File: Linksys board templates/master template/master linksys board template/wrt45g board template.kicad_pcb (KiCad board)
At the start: 2 copper layers, 160 x 138 mm, 98 parts, among them J1 RJ45, J2 RJ45, J3 RJ45, J4 RJ45, J5 RJ45, J6 Barrel_Jack_Switch, J7 switched ground, SW1 SW_Push, SW2 SW_Push, U1 AMS1117-3.3, U2 AMS1117-5.0, U3 YAAJ_DCDC_StepDown_LM2596

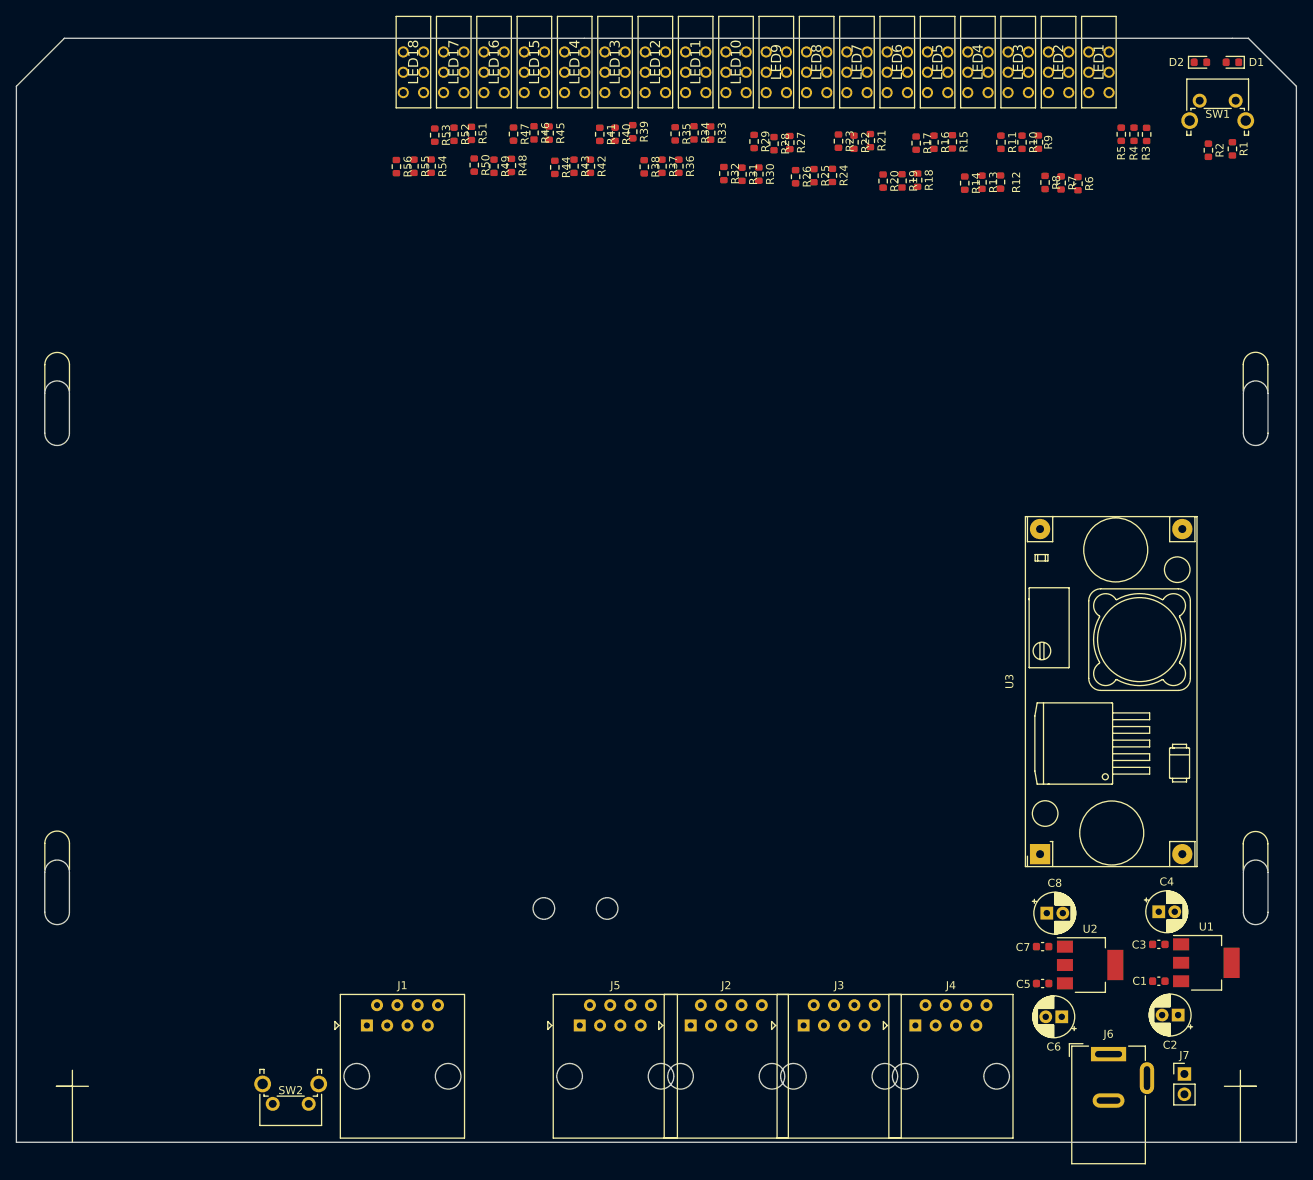
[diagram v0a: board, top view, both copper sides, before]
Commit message: tweaks to locations based on 1:1 printouts
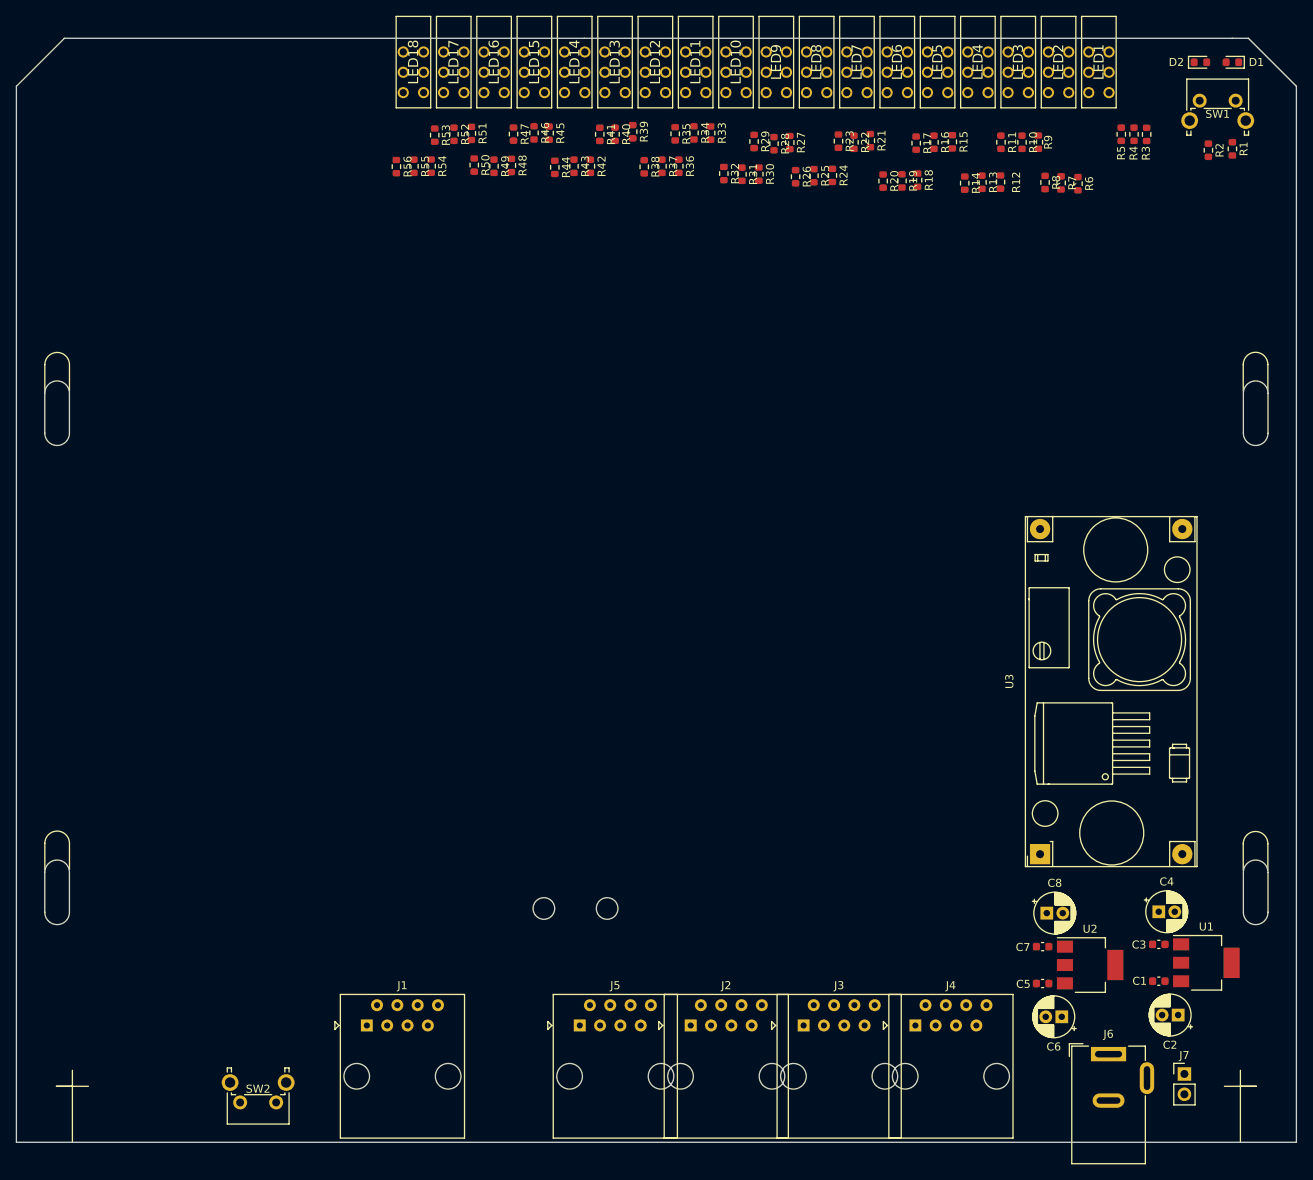
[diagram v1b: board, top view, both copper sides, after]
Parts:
- moved SW2 4.07 mm to (99.5, 155.0)
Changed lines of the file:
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@@
   )
   (footprint "Button_Switch_THT:SW_Tactile_SPST_Angled_PTS645Vx58-2LFS" (layer "F.Cu")
-    (at 103.54 155.2 180)
+    (at 99.47 155.02 180)
     (descr "tactile switch SPST right angle, PTS645VL58-2 LFS")
     (tags "tactile switch SPST angled PTS645VL58-2 LFS C&K Button")
@@
   (gr_line (start 223.435034 126) (end 223.435034 122.689649) (layer "F.SilkS") (width 0.1))
   (gr_line (start 220 160) (end 220 153) (layer "F.SilkS") (width 0.15))
-  (gr_arc (start 70.555001 62.8) (mid 72.1 61.270348) (end 73.635033 62.81) (layer "F.SilkS") (width 0.1))
+  (gr_arc (start 70.555001 62.8) (mid 72.1 61.270347) (end 73.635033 62.81) (layer "F.SilkS") (width 0.1))
   (gr_line (start 220 153) (end 220 151) (layer "F.SilkS") (width 0.15))
   (gr_line (start 74 153) (end 74 151) (layer "F.SilkS") (width 0.15))
   (gr_line (start 220.355002 126) (end 220.355002 122.679649) (layer "F.SilkS") (width 0.1))
   (gr_line (start 70.555001 66.120351) (end 70.555001 62.8) (layer "F.SilkS") (width 0.1))
-  (gr_arc (start 220.355001 62.779649) (mid 221.9 61.249998) (end 223.435033 62.789649) (layer "F.SilkS") (width 0.1))
+  (gr_arc (start 220.355001 62.779649) (mid 221.9 61.249997) (end 223.435033 62.789649) (layer "F.SilkS") (width 0.1))
   (gr_line (start 220 153) (end 222 153) (layer "F.SilkS") (width 0.15))
   (gr_line (start 73.635033 125.950002) (end 73.635033 122.639651) (layer "F.SilkS") (width 0.1))
   (gr_line (start 73.635033 66.120351) (end 73.635033 62.81) (layer "F.SilkS") (width 0.1))
-  (gr_arc (start 220.355002 122.679649) (mid 221.900001 121.149999) (end 223.435034 122.689649) (layer "F.SilkS") (width 0.1))
+  (gr_arc (start 220.355002 122.679649) (mid 221.900001 121.149998) (end 223.435034 122.689649) (layer "F.SilkS") (width 0.1))
   (gr_line (start 223.435033 66.1) (end 223.435033 62.789649) (layer "F.SilkS") (width 0.1))
-  (gr_arc (start 70.555001 122.629651) (mid 72.1 121.099999) (end 73.635033 122.639651) (layer "F.SilkS") (width 0.1))
+  (gr_arc (start 70.555001 122.629651) (mid 72.1 121.099998) (end 73.635033 122.639651) (layer "F.SilkS") (width 0.1))
   (gr_line (start 70.555001 125.950002) (end 70.555001 122.629651) (layer "F.SilkS") (width 0.1))
   (gr_line (start 222 153) (end 218 153) (layer "F.SilkS") (width 0.15))
